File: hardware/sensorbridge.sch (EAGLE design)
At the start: 19 parts, among them X1 1503_11, X2 1503_11, X3 1503_11, X4 1503_11, X5 1503_11, X6 1503_11

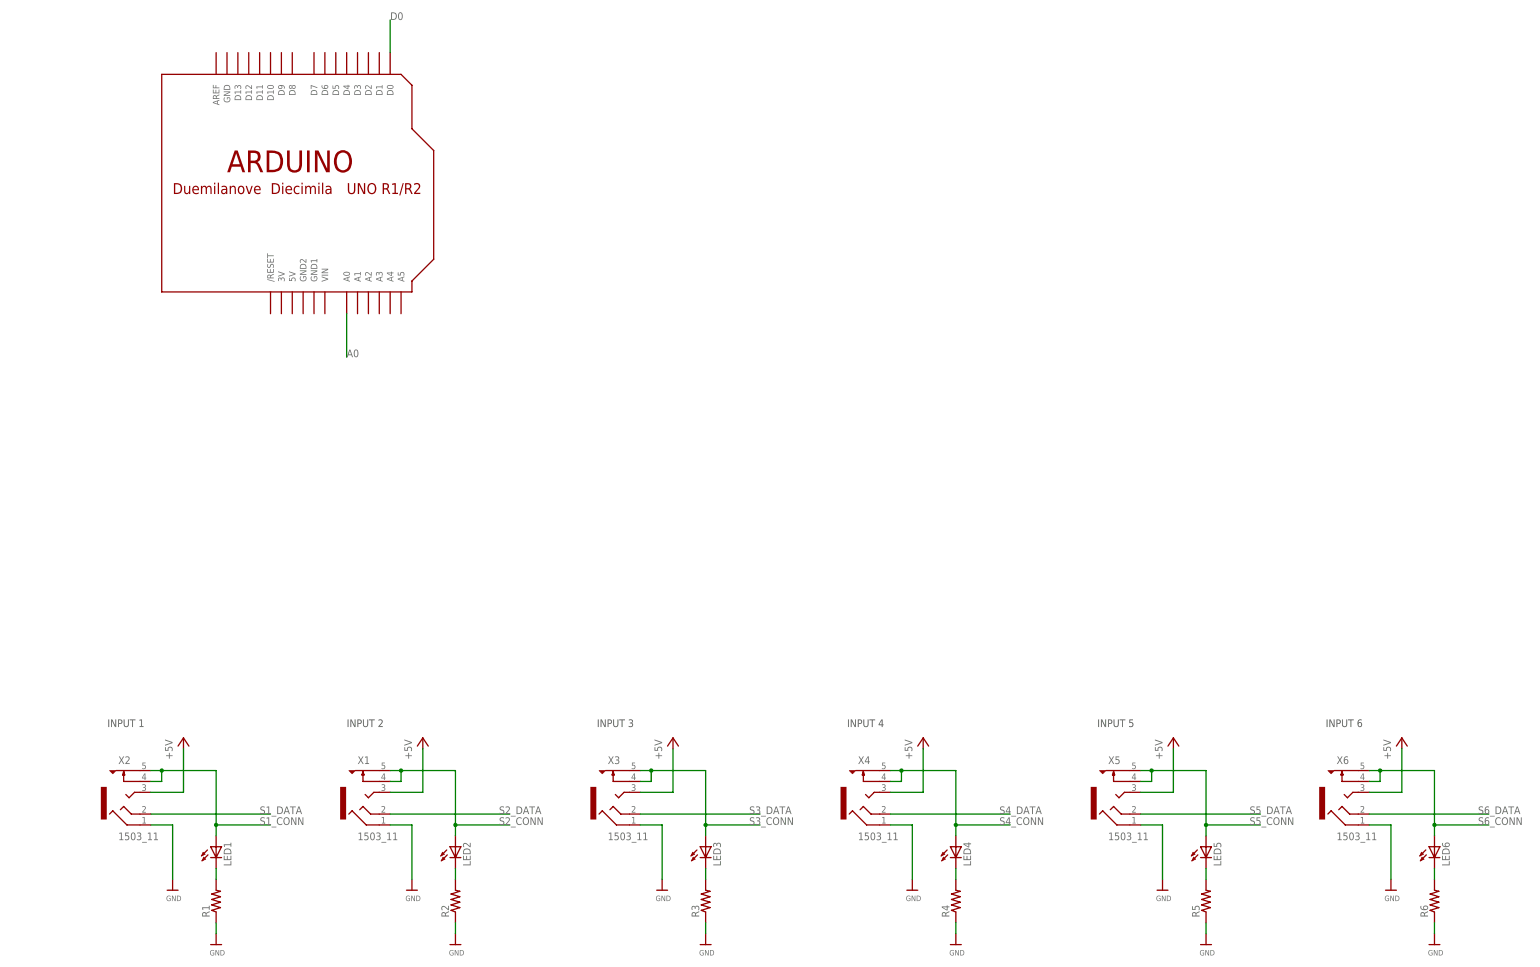
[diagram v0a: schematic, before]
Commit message: Updated board layout, replaced jack, added status led
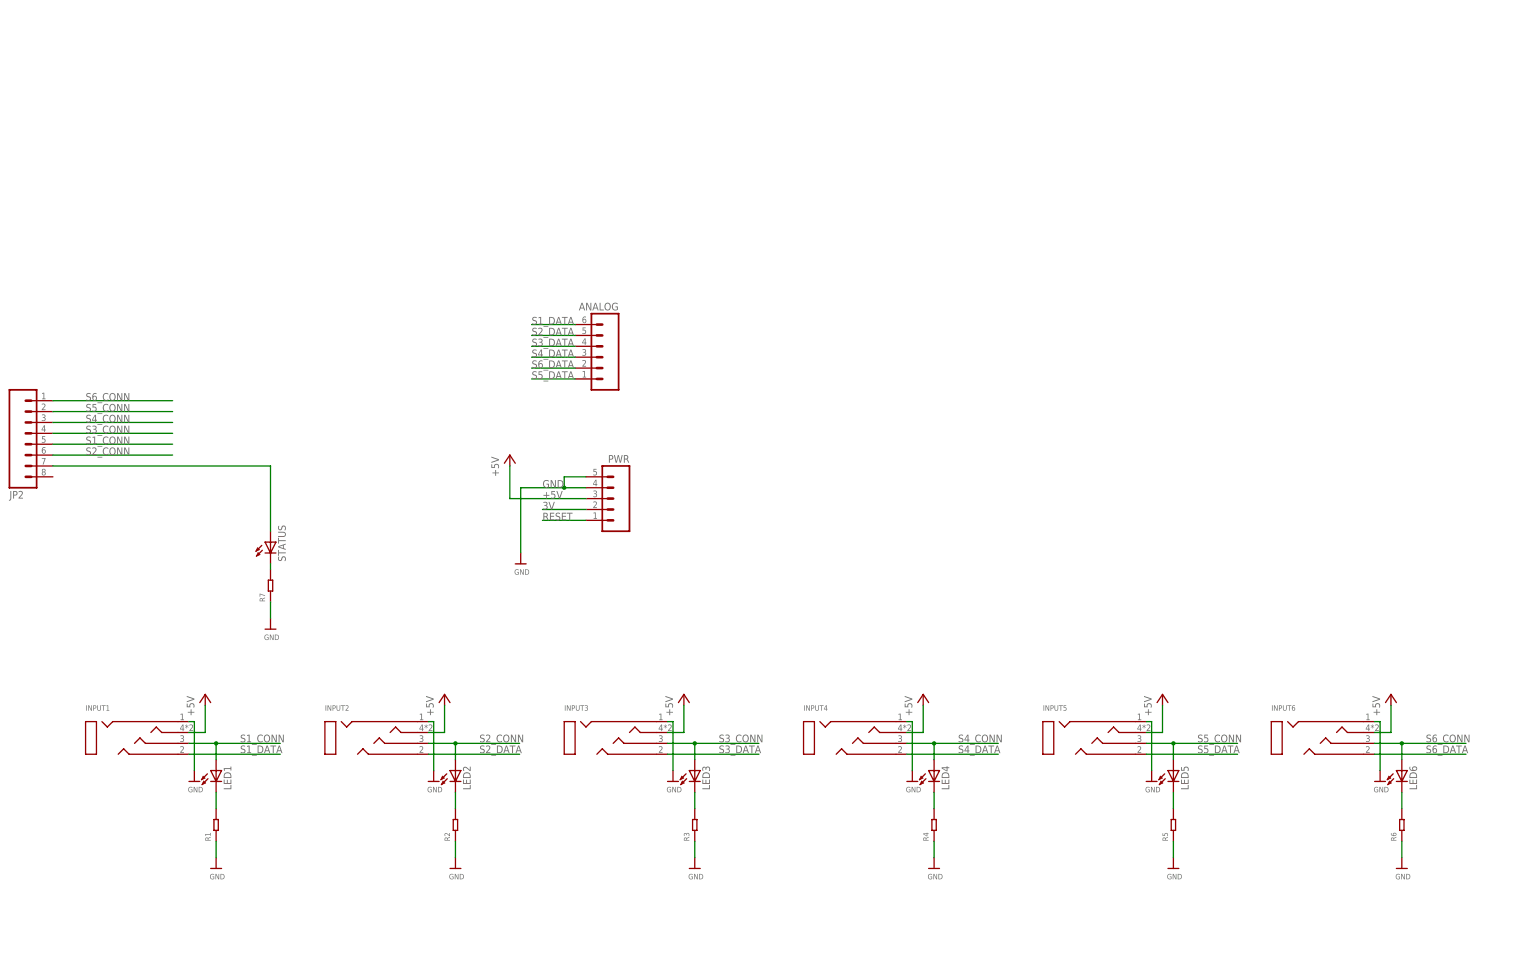
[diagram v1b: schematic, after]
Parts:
- removed U$2: ARDUINO-NOHOLE, adafruit:ARDUINO-NOHOLE
- removed X1, X2, X3, X4, X5, X6: 1503_11, con-lumberg:1503_11
- added ANALOG: (no value), SparkFun-Connectors:M06NO_SILK_FEMALE_PTH
- added INPUT1, INPUT2, INPUT3, INPUT4, INPUT5, INPUT6: MJ-2135, sensorlab:MJ-2135
- added JP2: (no value), SparkFun-Connectors:M08NO_SILK_FEMALE_PTH
- added PWR: (no value), SparkFun-Connectors:M05NO_SILK
- added R7: (no value), Seeed-OPL-Resistor:RES-0603
- added STATUS: (no value), adafruit:LEDCHIP-LED0603
- R1, R2, R3, R4, R5, R6: device adafruit:R-US_R0603 -> Seeed-OPL-Resistor:RES-0603
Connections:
- removed net A0: U$2.A0
- removed net D0: U$2.D0
- new net 3V: PWR.2
- new net N$7: R7.2, STATUS.C
- new net N$8: JP2.7, STATUS.A
- new net RESET: PWR.1
- net +5V: now also INPUT1.4, INPUT2.4, INPUT3.4, INPUT4.4, INPUT5.4, INPUT6.4, PWR.3; no longer X1.3, X2.3, X3.3, X4.3, X5.3, X6.3
- net GND: now also INPUT1.1, INPUT2.1, INPUT3.1, INPUT4.1, INPUT5.1, INPUT6.1, PWR.4, PWR.5, R7.1; no longer X1.1, X2.1, X3.1, X4.1, X5.1, X6.1
- net S1_CONN: now also INPUT1.3, JP2.5; no longer X2.4, X2.5
- net S1_DATA: now also ANALOG.6, INPUT1.2; no longer X2.2
- net S2_CONN: now also INPUT2.3, JP2.6; no longer X1.4, X1.5
- net S2_DATA: now also ANALOG.5, INPUT2.2; no longer X1.2
- net S3_CONN: now also INPUT3.3, JP2.4; no longer X3.4, X3.5
- net S3_DATA: now also ANALOG.4, INPUT3.2; no longer X3.2
- net S4_CONN: now also INPUT4.3, JP2.3; no longer X4.4, X4.5
- net S4_DATA: now also ANALOG.3, INPUT4.2; no longer X4.2
- net S5_CONN: now also INPUT5.3, JP2.2; no longer X5.4, X5.5
- net S5_DATA: now also ANALOG.1, INPUT5.2; no longer X5.2
- net S6_CONN: now also INPUT6.3, JP2.1; no longer X6.4, X6.5
- net S6_DATA: now also ANALOG.2, INPUT6.2; no longer X6.2
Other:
- note removed: "INPUT 1"
- note removed: "INPUT 2"
- note removed: "INPUT 3"
- note removed: "INPUT 4"
- note removed: "INPUT 5"
- note removed: "INPUT 6"
- moved on the sheet: LED1, LED2, LED3, LED4, LED5, LED6

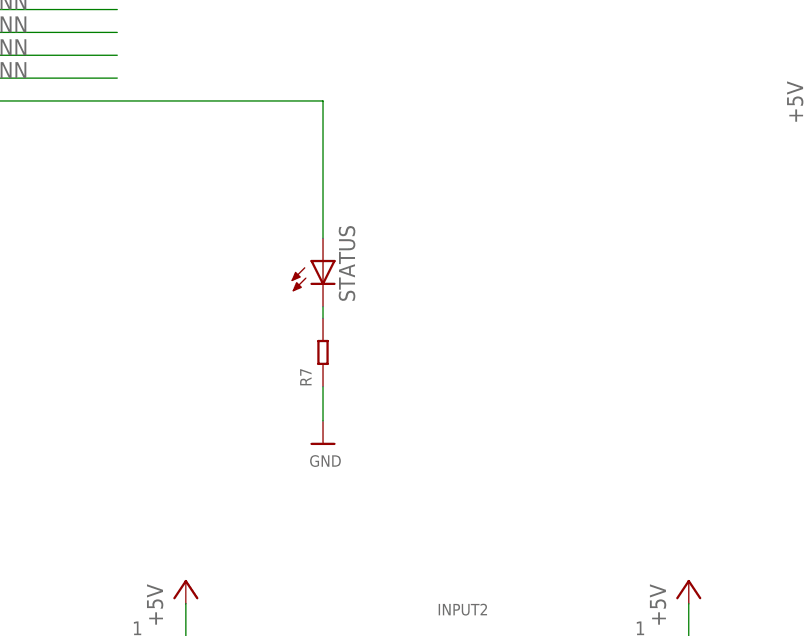
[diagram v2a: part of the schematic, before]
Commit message: Added power led
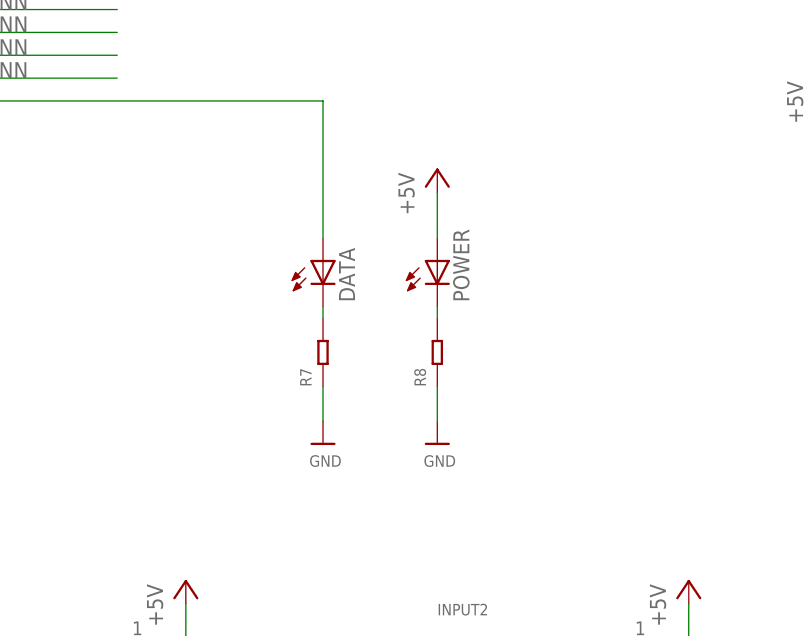
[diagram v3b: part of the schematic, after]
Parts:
- added POWER: (no value), adafruit:LEDCHIP-LED0603
- added R8: (no value), Seeed-OPL-Resistor:RES-0603
- renumbered STATUS to DATA
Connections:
- new net N$9: POWER.C, R8.2
- net +5V: now also POWER.A
- net GND: now also R8.1
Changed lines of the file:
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@@
 <part name="JP2" library="SparkFun-Connectors" deviceset="M08" device="NO_SILK_FEMALE_PTH"/>
 <part name="PWR" library="SparkFun-Connectors" deviceset="M05" device="NO_SILK"/>
-<part name="STATUS" library="adafruit" deviceset="LED" device="CHIP-LED0603"/>
+<part name="DATA" library="adafruit" deviceset="LED" device="CHIP-LED0603"/>
 <part name="R7" library="Seeed-OPL-Resistor" deviceset="RES" device="-0603"/>
 <part name="U$2" library="microbuilder" deviceset="GND" device=""/>
+<part name="POWER" library="adafruit" deviceset="LED" device="CHIP-LED0603"/>
+<part name="R8" library="Seeed-OPL-Resistor" deviceset="RES" device="-0603"/>
+<part name="U$15" library="microbuilder" deviceset="GND" device=""/>
+<part name="P+8" library="supply1" deviceset="+5V" device=""/>
 </parts>
 <sheets>
@@
 <instance part="JP2" gate="G$1" x="-10.16" y="60.96" rot="MR180"/>
 <instance part="PWR" gate="G$1" x="127" y="45.72" rot="MR0"/>
-<instance part="STATUS" gate="G$1" x="45.72" y="35.56"/>
+<instance part="DATA" gate="G$1" x="45.72" y="35.56"/>
 <instance part="R7" gate="R" x="45.72" y="25.4" rot="R90"/>
 <instance part="U$2" gate="G$1" x="45.72" y="15.24"/>
+<instance part="POWER" gate="G$1" x="58.42" y="35.56"/>
+<instance part="R8" gate="R" x="58.42" y="25.4" rot="R90"/>
+<instance part="U$15" gate="G$1" x="58.42" y="15.24"/>
+<instance part="P+8" gate="1" x="58.42" y="45.72"/>
 </instances>
 <busses>
@@
 <wire x1="45.72" y1="17.78" x2="45.72" y2="21.59" width="0.1524" layer="91"/>
 </segment>
+<segment>
+<pinref part="U$15" gate="G$1" pin="GND"/>
+<pinref part="R8" gate="R" pin="1"/>
+<wire x1="58.42" y1="21.59" x2="58.42" y2="17.78" width="0.1524" layer="91"/>
+</segment>
 </net>
 <net name="N$1" class="0">
@@
 <label x="109.22" y="45.72" size="1.778" layer="95"/>
 <pinref part="PWR" gate="G$1" pin="3"/>
+</segment>
+<segment>
+<pinref part="P+8" gate="1" pin="+5V"/>
+<pinref part="POWER" gate="G$1" pin="A"/>
+<wire x1="58.42" y1="43.18" x2="58.42" y2="38.1" width="0.1524" layer="91"/>
 </segment>
 </net>
@@
 <segment>
 <pinref part="R7" gate="R" pin="2"/>
-<pinref part="STATUS" gate="G$1" pin="C"/>
+<pinref part="DATA" gate="G$1" pin="C"/>
 <wire x1="45.72" y1="29.21" x2="45.72" y2="30.48" width="0.1524" layer="91"/>
 </segment>
@@
 <pinref part="JP2" gate="G$1" pin="7"/>
 <wire x1="-5.08" y1="53.34" x2="45.72" y2="53.34" width="0.1524" layer="91"/>
-<pinref part="STATUS" gate="G$1" pin="A"/>
+<pinref part="DATA" gate="G$1" pin="A"/>
 <wire x1="45.72" y1="53.34" x2="45.72" y2="38.1" width="0.1524" layer="91"/>
 </segment>
 </net>
+<net name="N$9" class="0">
+<segment>
+<pinref part="POWER" gate="G$1" pin="C"/>
+<wire x1="58.42" y1="30.48" x2="58.42" y2="29.21" width="0.1524" layer="91"/>
+<pinref part="R8" gate="R" pin="2"/>
+</segment>
+</net>

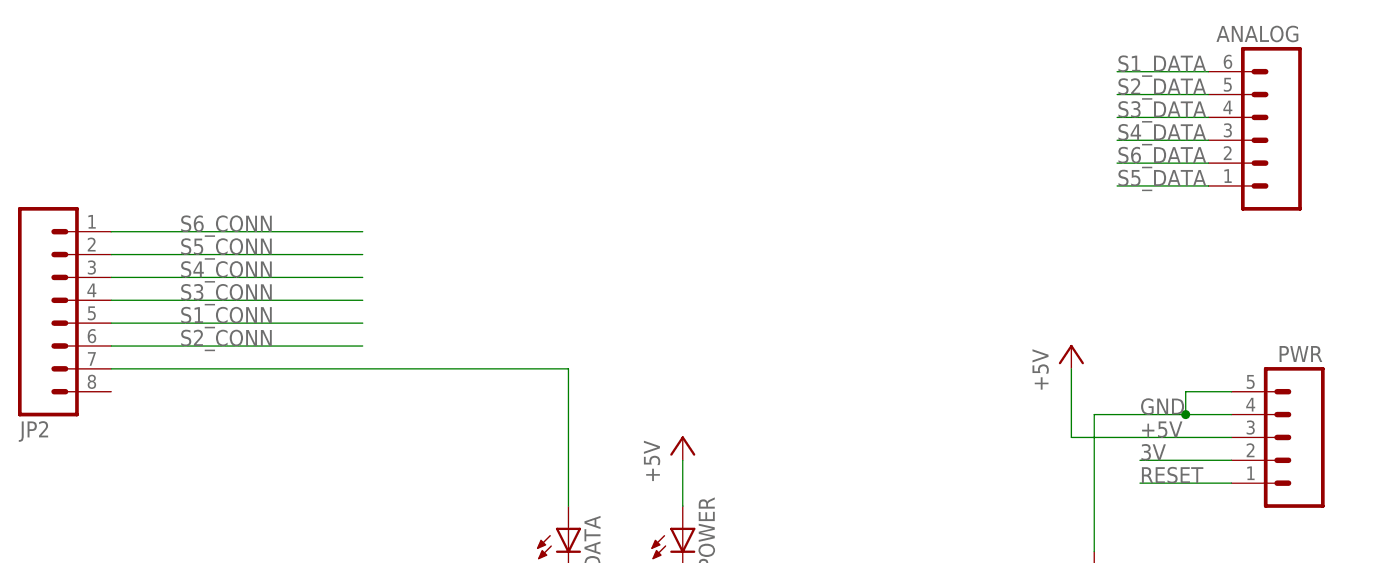
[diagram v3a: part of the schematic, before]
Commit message: Added arduino pin names to info layer
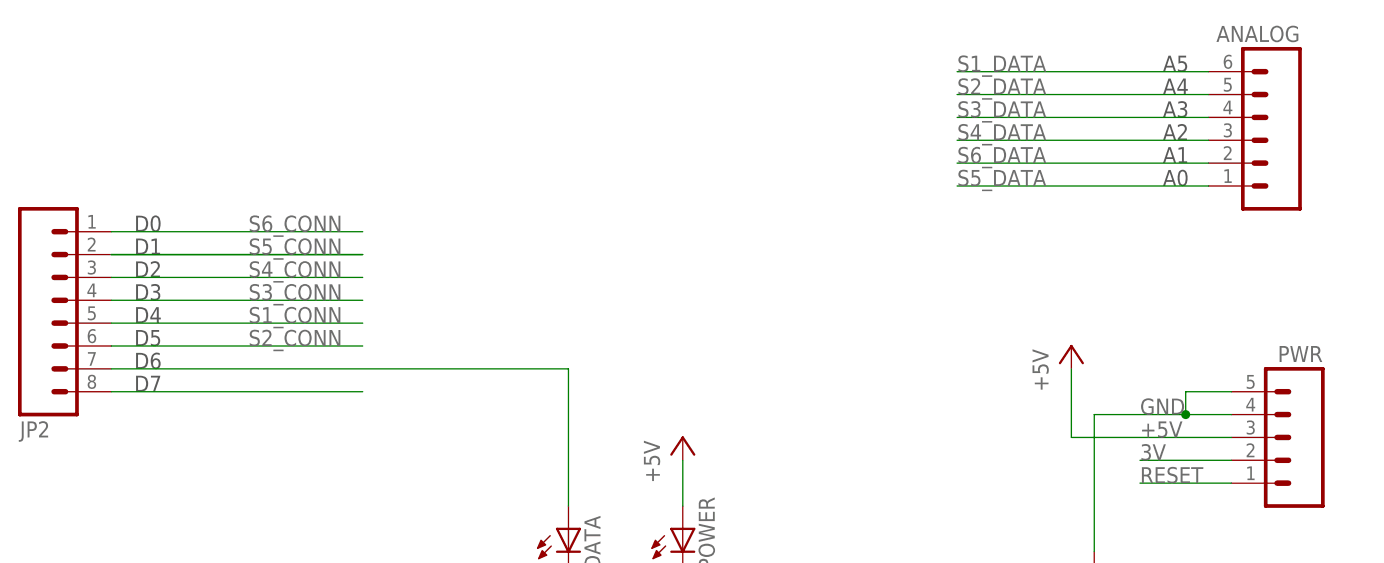
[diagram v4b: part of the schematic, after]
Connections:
- new net N$10: JP2.8
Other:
- note added: "A0"
- note added: "A1"
- note added: "A2"
- note added: "A3"
- note added: "A4"
- note added: "A5"
- note added: "D0"
- note added: "D1"
- note added: "D2"
- note added: "D3"
- note added: "D4"
- note added: "D5"
- note added: "D6"
- note added: "D7"
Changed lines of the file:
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@@
 <sheet>
 <plain>
+<text x="111.76" y="73.66" size="1.778" layer="97">A0</text>
+<text x="111.76" y="76.2" size="1.778" layer="97">A1</text>
+<text x="111.76" y="78.74" size="1.778" layer="97">A2</text>
+<text x="111.76" y="81.28" size="1.778" layer="97">A3</text>
+<text x="111.76" y="83.82" size="1.778" layer="97">A4</text>
+<text x="111.76" y="86.36" size="1.778" layer="97">A5</text>
+<text x="-2.54" y="68.58" size="1.778" layer="97">D0</text>
+<text x="-2.54" y="66.04" size="1.778" layer="97">D1</text>
+<text x="-2.54" y="63.5" size="1.778" layer="97">D2</text>
+<text x="-2.54" y="60.96" size="1.778" layer="97">D3</text>
+<text x="-2.54" y="58.42" size="1.778" layer="97">D4</text>
+<text x="-2.54" y="55.88" size="1.778" layer="97">D5</text>
+<text x="-2.54" y="53.34" size="1.778" layer="97">D6</text>
+<text x="-2.54" y="50.8" size="1.778" layer="97">D7</text>
 </plain>
 <instances>
@@
 </segment>
 <segment>
-<label x="2.54" y="58.42" size="1.778" layer="95"/>
+<label x="10.16" y="58.42" size="1.778" layer="95"/>
 <pinref part="JP2" gate="G$1" pin="5"/>
 <wire x1="22.86" y1="58.42" x2="-5.08" y2="58.42" width="0.1524" layer="91"/>
@@
 </segment>
 <segment>
-<label x="106.68" y="86.36" size="1.778" layer="95"/>
+<label x="88.9" y="86.36" size="1.778" layer="95"/>
 <pinref part="ANALOG" gate="G$1" pin="6"/>
-<wire x1="106.68" y1="86.36" x2="116.84" y2="86.36" width="0.1524" layer="91"/>
+<wire x1="88.9" y1="86.36" x2="116.84" y2="86.36" width="0.1524" layer="91"/>
 </segment>
 </net>
@@
 </segment>
 <segment>
-<label x="2.54" y="55.88" size="1.778" layer="95"/>
+<label x="10.16" y="55.88" size="1.778" layer="95"/>
 <pinref part="JP2" gate="G$1" pin="6"/>
 <wire x1="22.86" y1="55.88" x2="-5.08" y2="55.88" width="0.1524" layer="91"/>
@@
 </segment>
 <segment>
-<label x="106.68" y="83.82" size="1.778" layer="95"/>
+<label x="88.9" y="83.82" size="1.778" layer="95"/>
 <pinref part="ANALOG" gate="G$1" pin="5"/>
-<wire x1="106.68" y1="83.82" x2="116.84" y2="83.82" width="0.1524" layer="91"/>
+<wire x1="88.9" y1="83.82" x2="116.84" y2="83.82" width="0.1524" layer="91"/>
 </segment>
 </net>
@@
 </segment>
 <segment>
-<label x="2.54" y="60.96" size="1.778" layer="95"/>
+<label x="10.16" y="60.96" size="1.778" layer="95"/>
 <pinref part="JP2" gate="G$1" pin="4"/>
 <wire x1="22.86" y1="60.96" x2="-5.08" y2="60.96" width="0.1524" layer="91"/>
@@
 </segment>
 <segment>
-<label x="106.68" y="81.28" size="1.778" layer="95"/>
+<label x="88.9" y="81.28" size="1.778" layer="95"/>
 <pinref part="ANALOG" gate="G$1" pin="4"/>
-<wire x1="106.68" y1="81.28" x2="116.84" y2="81.28" width="0.1524" layer="91"/>
+<wire x1="88.9" y1="81.28" x2="116.84" y2="81.28" width="0.1524" layer="91"/>
 </segment>
 </net>
@@
 </segment>
 <segment>
-<label x="2.54" y="63.5" size="1.778" layer="95"/>
+<label x="10.16" y="63.5" size="1.778" layer="95"/>
 <pinref part="JP2" gate="G$1" pin="3"/>
 <wire x1="22.86" y1="63.5" x2="-5.08" y2="63.5" width="0.1524" layer="91"/>
@@
 </segment>
 <segment>
-<label x="106.68" y="78.74" size="1.778" layer="95"/>
+<label x="88.9" y="78.74" size="1.778" layer="95"/>
 <pinref part="ANALOG" gate="G$1" pin="3"/>
-<wire x1="106.68" y1="78.74" x2="116.84" y2="78.74" width="0.1524" layer="91"/>
+<wire x1="88.9" y1="78.74" x2="116.84" y2="78.74" width="0.1524" layer="91"/>
 </segment>
 </net>
@@
 <segment>
 <wire x1="-5.08" y1="66.04" x2="22.86" y2="66.04" width="0.1524" layer="91"/>
-<label x="2.54" y="66.04" size="1.778" layer="95"/>
+<label x="10.16" y="66.04" size="1.778" layer="95"/>
 <pinref part="JP2" gate="G$1" pin="2"/>
+<wire x1="-5.08" y1="66.04" x2="22.86" y2="66.04" width="0.1524" layer="91"/>
 </segment>
 </net>
@@
 </segment>
 <segment>
-<label x="106.68" y="73.66" size="1.778" layer="95"/>
+<label x="88.9" y="73.66" size="1.778" layer="95"/>
 <pinref part="ANALOG" gate="G$1" pin="1"/>
-<wire x1="106.68" y1="73.66" x2="116.84" y2="73.66" width="0.1524" layer="91"/>
+<wire x1="88.9" y1="73.66" x2="116.84" y2="73.66" width="0.1524" layer="91"/>
 </segment>
 </net>
@@
 </segment>
 <segment>
-<label x="2.54" y="68.58" size="1.778" layer="95"/>
+<label x="10.16" y="68.58" size="1.778" layer="95"/>
 <pinref part="JP2" gate="G$1" pin="1"/>
 <wire x1="22.86" y1="68.58" x2="-5.08" y2="68.58" width="0.1524" layer="91"/>
@@
 </segment>
 <segment>
-<label x="106.68" y="76.2" size="1.778" layer="95"/>
+<label x="88.9" y="76.2" size="1.778" layer="95"/>
 <pinref part="ANALOG" gate="G$1" pin="2"/>
-<wire x1="106.68" y1="76.2" x2="116.84" y2="76.2" width="0.1524" layer="91"/>
+<wire x1="88.9" y1="76.2" x2="116.84" y2="76.2" width="0.1524" layer="91"/>
 </segment>
 </net>
@@
 </segment>
 </net>
+<net name="N$10" class="0">
+<segment>
+<pinref part="JP2" gate="G$1" pin="8"/>
+<wire x1="-5.08" y1="50.8" x2="22.86" y2="50.8" width="0.1524" layer="91"/>
+</segment>
+</net>
